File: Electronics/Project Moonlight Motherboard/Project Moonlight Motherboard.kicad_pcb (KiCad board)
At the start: 2 copper layers, 104.9 x 56.3 mm, 31 parts, among them CN10 B2B-XH-A, CN11 B2B-XH-A, CN12 B2B-XH-A, CN5 1751248, CN6 1751248, CN7 B2B-XH-A, CN8 B2B-XH-A, CN9 B2B-XH-A, Q1 AO3400A, Q2 AO3400A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

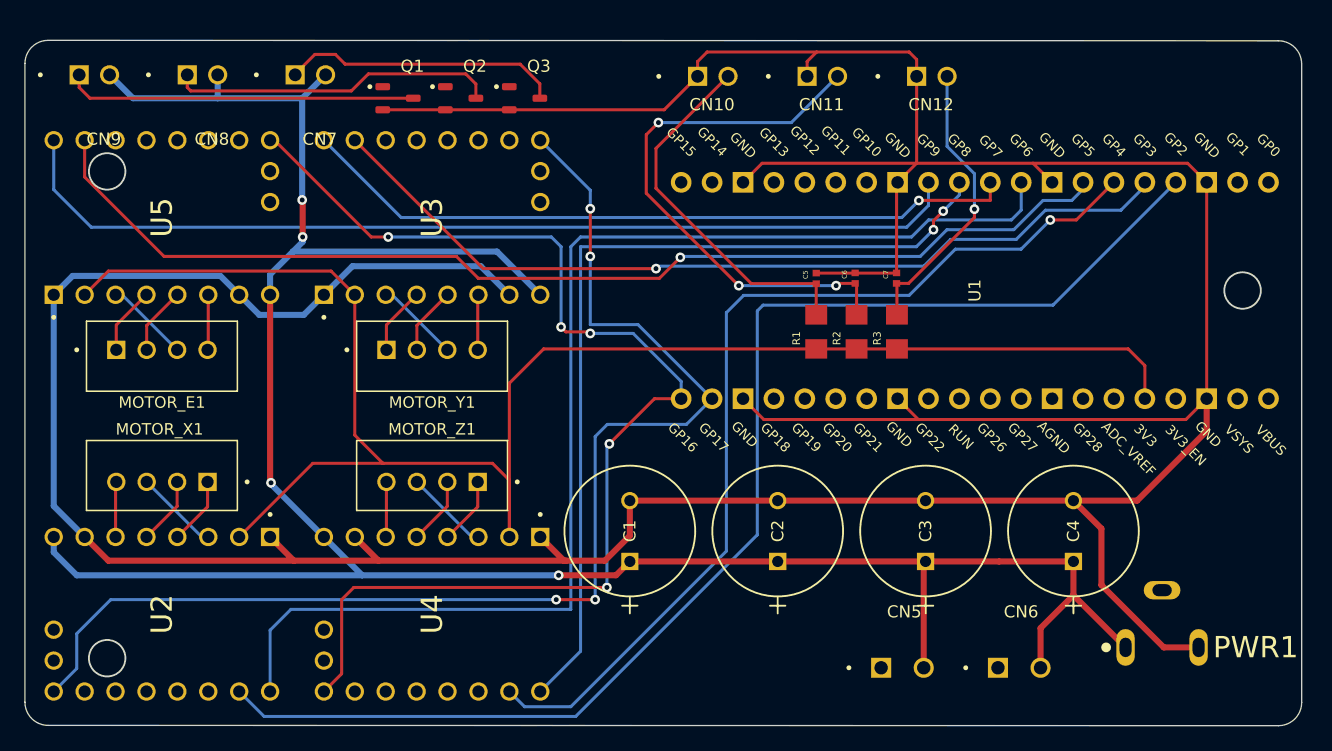
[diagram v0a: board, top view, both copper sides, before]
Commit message: reorganized schematic and updated refs + routing
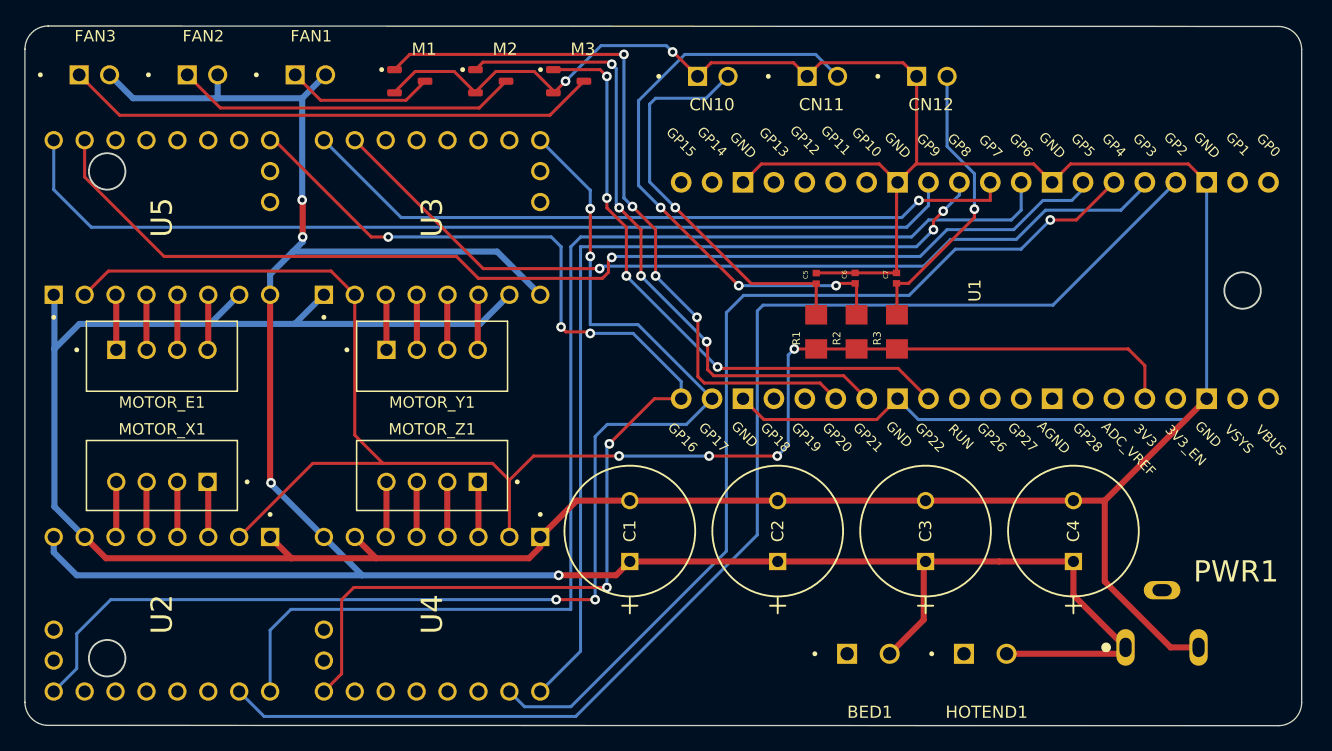
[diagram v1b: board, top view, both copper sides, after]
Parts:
- removed Q1, Q2, Q3: AO3400A, AO3400A:SOT95P280X125-3N
- added M1: AO3400A, AO3400A:SOT95P280X125-3N, F.Cu at (132.6, 73.2)
- added M2: AO3400A, AO3400A:SOT95P280X125-3N, F.Cu at (139.3, 73.2)
- added M3: AO3400A, AO3400A:SOT95P280X125-3N, F.Cu at (145.7, 73.2)
- moved BED1 3.02 mm to (166.5, 123.8)
- moved HOTEND1 3.02 mm to (176.1, 123.8)
- renumbered CN5 to BED1, CN7 to FAN1, CN8 to FAN2, CN9 to FAN3, CN6 to HOTEND1
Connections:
- MOTOR_E1 pad 1: Net-(U5-M1A) -> Net-(U5-M1B)
- MOTOR_E1 pad 2: Net-(U5-M2A) -> Net-(U5-M1A)
- MOTOR_E1 pad 3: Net-(U5-M1B) -> Net-(U5-M2A)
- MOTOR_X1 pad 1: Net-(U2-M1A) -> Net-(U2-M1B)
- MOTOR_X1 pad 2: Net-(U2-M2A) -> Net-(U2-M1A)
- MOTOR_X1 pad 3: Net-(U2-M1B) -> Net-(U2-M2A)
- MOTOR_Y1 pad 1: Net-(U3-M1A) -> Net-(U3-M1B)
- MOTOR_Y1 pad 2: Net-(U3-M2A) -> Net-(U3-M1A)
- MOTOR_Y1 pad 3: Net-(U3-M1B) -> Net-(U3-M2A)
- MOTOR_Z1 pad 1: Net-(U4-M1A) -> Net-(U4-M1B)
- MOTOR_Z1 pad 2: Net-(U4-M2A) -> Net-(U4-M1A)
- MOTOR_Z1 pad 3: Net-(U4-M1B) -> Net-(U4-M2A)
- U1 pad 26: unconnected-(U1-GPIO20-Pad26) -> Net-(U1-GPIO20)
- U1 pad 27: unconnected-(U1-GPIO21-Pad27) -> Net-(U1-GPIO21)
- U1 pad 29: unconnected-(U1-GPIO22-Pad29) -> Net-(U1-GPIO22)
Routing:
- net Net-(U1-GPIO20): track 0.00 -> 60.4 mm, vias 0 -> 4
- net Net-(U1-GPIO21): track 0.00 -> 53.9 mm, vias 0 -> 4
- net Net-(U1-GPIO22): track 0.00 -> 50.7 mm, vias 0 -> 4
- net Net-(FAN3-Pad1): track 28.9 -> 44.4 mm
- net Net-(FAN1-Pad1): track 23.0 -> 12.2 mm
- net GNDREF: track 366.3 -> 359.7 mm, vias 0 -> 2
- net +3V3: track 137.9 -> 132.9 mm, vias 0 -> 4
- net Net-(C6-Pad1): track 45.5 -> 49.6 mm
- net VCC: track 198.0 -> 201.0 mm
- net Net-(C5-Pad1): track 30.6 -> 33.5 mm, vias 0 -> 1
- net Net-(U5-M1B): track 6.93 -> 4.55 mm
- net Net-(U4-M1B): track 6.93 -> 4.55 mm
- net Net-(U2-M1B): track 6.93 -> 4.55 mm
- net Net-(U3-M1B): track 6.93 -> 4.55 mm
- net Net-(FAN2-Pad1): track 27.0 -> 28.2 mm
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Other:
- board size 104.9 x 56.3 mm -> 104.9 x 57.5 mm

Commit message: added power MOSFETs for hotend and bed
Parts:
- added Q1: ~, IRFH7440TRPBF:TRANS_FDMS86202, F.Cu at (150.5, 122.2)
- added Q2: ~, IRFH7440TRPBF:TRANS_FDMS86202, F.Cu at (159.8, 122.2)
- renumbered CN10 to THM1, CN11 to THM2, CN12 to THM3
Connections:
- BED1 pad 01: unconnected-(BED1-Pad01) -> Net-(BED1-Pad01)
- HOTEND1 pad 01: unconnected-(HOTEND1-Pad01) -> Net-(HOTEND1-Pad01)
- U1 pad 24: unconnected-(U1-GPIO18-Pad24) -> Net-(Q1-G)
- U1 pad 25: unconnected-(U1-GPIO19-Pad25) -> Net-(Q2-G)
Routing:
- net GNDREF: track 359.7 -> 412.5 mm, vias 2 -> 4
- net Net-(Q1-G): track 0.00 -> 31.9 mm, vias 0 -> 1
- net Net-(HOTEND1-Pad01): track 0.00 -> 31.8 mm
- net Net-(Q2-G): track 0.00 -> 28.3 mm, vias 0 -> 1
- net Net-(BED1-Pad01): track 0.00 -> 13.4 mm
- net +3V3: track 132.9 -> 131.5 mm
- net Net-(U1-GPIO2): track 106.8 -> 108.1 mm
